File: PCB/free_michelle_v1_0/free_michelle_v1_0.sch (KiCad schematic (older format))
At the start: 2 parts

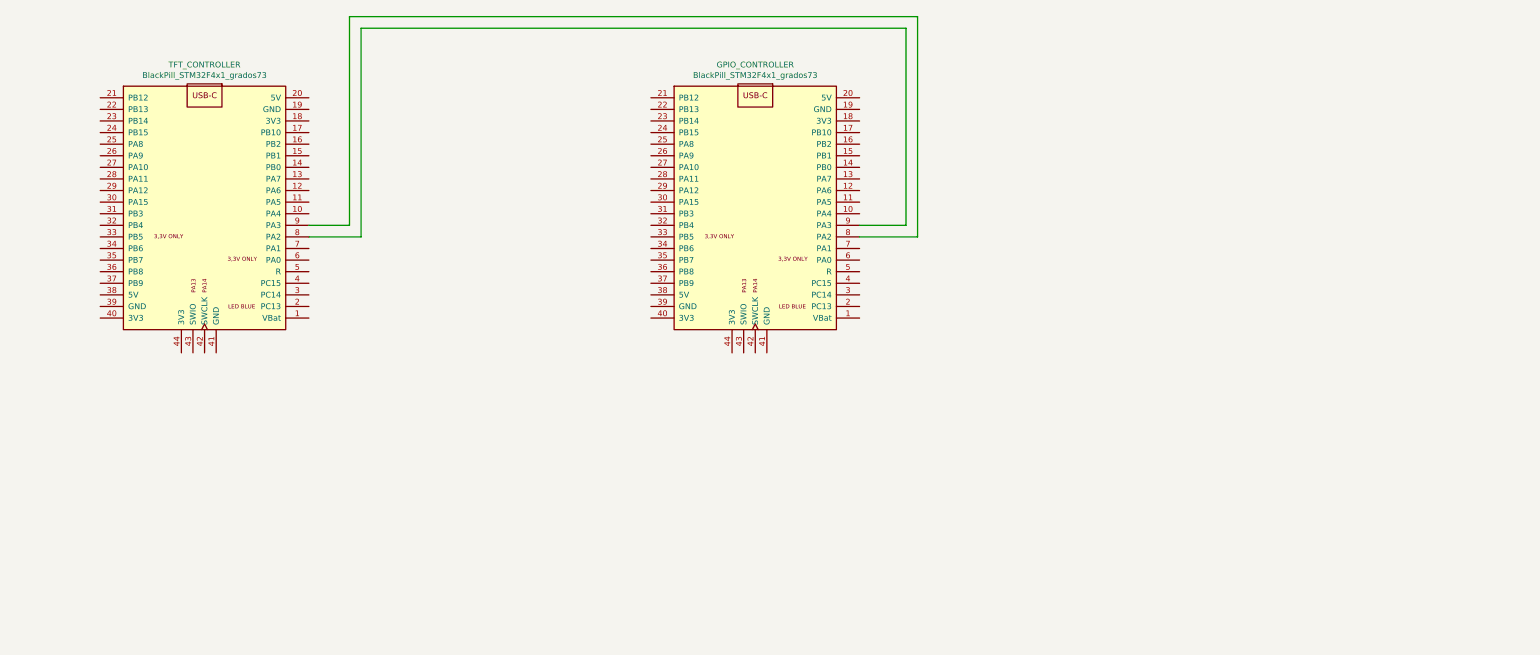
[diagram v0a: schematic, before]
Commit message: Dodano polaczenia pomiedzy uC a TFT
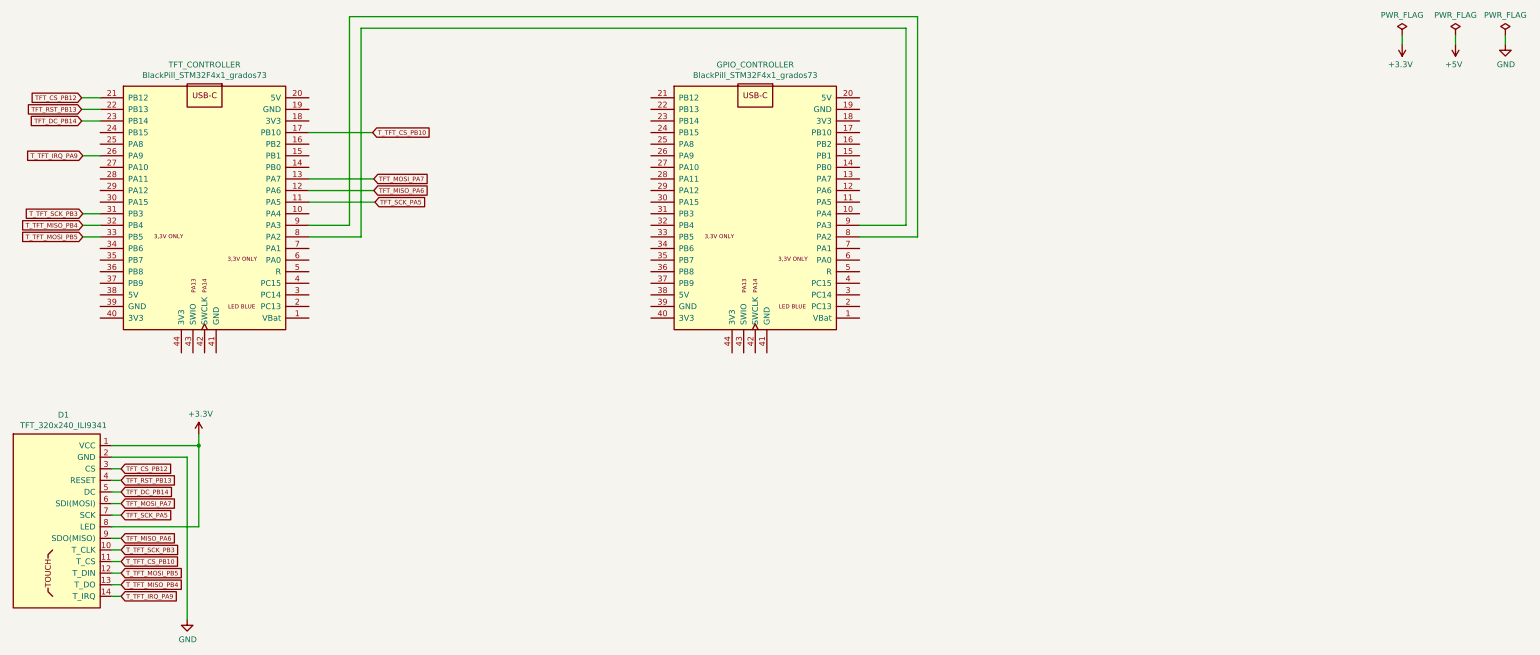
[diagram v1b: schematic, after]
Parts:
- added D1: TFT_320x240_ILI9341, symbol grad73_library:TFT_320x240_ILI9341
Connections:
- net TFT_SCK_PA5: now reaches TFT_CONTROLLER.11 (PA5)
- net TFT_SCK_PA5: now also D1.7 (SCK)
- net TFT_MISO_PA6: now reaches TFT_CONTROLLER.12 (PA6)
- net TFT_MISO_PA6: now also D1.9 (SDO(MISO))
- net TFT_MOSI_PA7: now reaches TFT_CONTROLLER.13 (PA7)
- net TFT_MOSI_PA7: now also D1.6 (SDI(MOSI))
- net T_TFT_CS_PB10: now reaches TFT_CONTROLLER.17 (PB10)
- net T_TFT_CS_PB10: now also D1.11 (T_CS)
- net TFT_CS_PB12: now reaches TFT_CONTROLLER.21 (PB12)
- net TFT_CS_PB12: now also D1.3 (CS)
- net TFT_RST_PB13: now reaches TFT_CONTROLLER.22 (PB13)
- net TFT_RST_PB13: now also D1.4 (RESET)
- net TFT_DC_PB14: now reaches TFT_CONTROLLER.23 (PB14)
- net TFT_DC_PB14: now also D1.5 (DC)
- net T_TFT_IRQ_PA9: now reaches TFT_CONTROLLER.26 (PA9)
- net T_TFT_IRQ_PA9: now also D1.14 (T_IRQ)
- net T_TFT_SCK_PB3: now reaches TFT_CONTROLLER.31 (PB3)
- net T_TFT_SCK_PB3: now also D1.10 (T_CLK)
- net T_TFT_MISO_PB4: now reaches TFT_CONTROLLER.32 (PB4)
- net T_TFT_MISO_PB4: now also D1.13 (T_DO)
- net T_TFT_MOSI_PB5: now reaches TFT_CONTROLLER.33 (PB5)
- net T_TFT_MOSI_PB5: now also D1.12 (T_DIN)
- new net +3V3: D1.1 (VCC), D1.8 (LED)
- new net GND: D1.2 (GND)
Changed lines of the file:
@@
 Wire Wire Line
 	8800 2800 8300 2800
+$Comp
+L grad73_library:TFT_320x240_ILI9341 D1
+U 1 1 61DB7F28
+P 1700 4400
+F 0 "D1" H 1433 4465 50  0000 C CNN
+F 1 "TFT_320x240_ILI9341" H 1433 4374 50  0000 C CNN
+F 2 "" H 1700 4400 50  0001 C CNN
+F 3 "" H 1700 4400 50  0001 C CNN
+	1    1700 4400
+	1    0    0    -1
+$EndComp
+$Comp
+L power:GND #PWR?
+U 1 1 61DBA788
+P 2500 6100
+F 0 "#PWR?" H 2500 5850 50  0001 C CNN
+F 1 "GND" H 2505 5927 50  0000 C CNN
+F 2 "" H 2500 6100 50  0001 C CNN
+F 3 "" H 2500 6100 50  0001 C CNN
+	1    2500 6100
+	1    0    0    -1
+$EndComp
+$Comp
+L power:+3.3V #PWR?
+U 1 1 61DBE35F
+P 2600 4500
+F 0 "#PWR?" H 2600 4350 50  0001 C CNN
+F 1 "+3.3V" H 2615 4673 50  0000 C CNN
+F 2 "" H 2600 4500 50  0001 C CNN
+F 3 "" H 2600 4500 50  0001 C CNN
+	1    2600 4500
+	1    0    0    -1
+$EndComp
+$Comp
+L power:PWR_FLAG #FLG?
+U 1 1 61DC06F2
+P 12980 1060
+F 0 "#FLG?" H 12980 1135 50  0001 C CNN
+F 1 "PWR_FLAG" H 12980 1233 50  0000 C CNN
+F 2 "" H 12980 1060 50  0001 C CNN
+F 3 "~" H 12980 1060 50  0001 C CNN
+	1    12980 1060
+	1    0    0    -1
+$EndComp
+$Comp
+L power:PWR_FLAG #FLG?
+U 1 1 61DC1287
+P 13440 1060
+F 0 "#FLG?" H 13440 1135 50  0001 C CNN
+F 1 "PWR_FLAG" H 13440 1233 50  0000 C CNN
+F 2 "" H 13440 1060 50  0001 C CNN
+F 3 "~" H 13440 1060 50  0001 C CNN
+	1    13440 1060
+	1    0    0    -1
+$EndComp
+$Comp
+L power:PWR_FLAG #FLG?
+U 1 1 61DC1D57
+P 13870 1060
+F 0 "#FLG?" H 13870 1135 50  0001 C CNN
+F 1 "PWR_FLAG" H 13870 1233 50  0000 C CNN
+F 2 "" H 13870 1060 50  0001 C CNN
+F 3 "~" H 13870 1060 50  0001 C CNN
+	1    13870 1060
+	1    0    0    -1
+$EndComp
+$Comp
+L power:+3.3V #PWR?
+U 1 1 61DC2834
+P 12980 1140
+F 0 "#PWR?" H 12980 990 50  0001 C CNN
+F 1 "+3.3V" H 12995 1313 50  0000 C CNN
+F 2 "" H 12980 1140 50  0001 C CNN
+F 3 "" H 12980 1140 50  0001 C CNN
+	1    12980 1140
+	-1   0    0    1
+$EndComp
+$Comp
+L power:+5V #PWR?
+U 1 1 61DC4ACB
+P 13440 1140
+F 0 "#PWR?" H 13440 990 50  0001 C CNN
+F 1 "+5V" H 13455 1313 50  0000 C CNN
+F 2 "" H 13440 1140 50  0001 C CNN
+F 3 "" H 13440 1140 50  0001 C CNN
+	1    13440 1140
+	-1   0    0    1
+$EndComp
+$Comp
+L power:GND #PWR?
+U 1 1 61DC5D3E
+P 13870 1140
+F 0 "#PWR?" H 13870 890 50  0001 C CNN
+F 1 "GND" H 13875 967 50  0000 C CNN
+F 2 "" H 13870 1140 50  0001 C CNN
+F 3 "" H 13870 1140 50  0001 C CNN
+	1    13870 1140
+	1    0    0    -1
+$EndComp
+Wire Wire Line
+	12980 1060 12980 1140
+Wire Wire Line
+	13440 1060 13440 1140
+Wire Wire Line
+	13870 1060 13870 1140
+Text GLabel 1930 4800 2    39   Input ~ 0
+TFT_CS_PB12
+Text GLabel 1590 1600 0    39   Input ~ 0
+TFT_CS_PB12
+Wire Wire Line
+	1590 1600 1750 1600
+Wire Wire Line
+	1850 4800 1930 4800
+Text GLabel 1930 4900 2    39   Input ~ 0
+TFT_RST_PB13
+Wire Wire Line
+	1850 4900 1930 4900
+Text GLabel 1590 1700 0    39   Input ~ 0
+TFT_RST_PB13
+Wire Wire Line
+	1590 1700 1750 1700
+Text GLabel 1930 5000 2    39   Input ~ 0
+TFT_DC_PB14
+Wire Wire Line
+	1930 5000 1850 5000
+Text GLabel 1590 1800 0    39   Input ~ 0
+TFT_DC_PB14
+Wire Wire Line
+	1590 1800 1750 1800
+Text GLabel 1930 5100 2    39   Input ~ 0
+TFT_MOSI_PA7
+Wire Wire Line
+	1930 5100 1850 5100
+Text GLabel 1930 5200 2    39   Input ~ 0
+TFT_SCK_PA5
+Wire Wire Line
+	1930 5200 1850 5200
+Text GLabel 4110 2300 2    39   Input ~ 0
+TFT_MOSI_PA7
+Wire Wire Line
+	4110 2300 3550 2300
+Text GLabel 4120 2500 2    39   Input ~ 0
+TFT_SCK_PA5
+Wire Wire Line
+	4120 2500 3550 2500
+Wire Wire Line
+	1850 4600 2600 4600
+Wire Wire Line
+	2600 4600 2600 4500
+Wire Wire Line
+	1850 5300 2600 5300
+Wire Wire Line
+	2600 5300 2600 4600
+Connection ~ 2600 4600
+Text GLabel 1930 5400 2    39   Input ~ 0
+TFT_MISO_PA6
+Wire Wire Line
+	1930 5400 1850 5400
+Text GLabel 4110 2400 2    39   Input ~ 0
+TFT_MISO_PA6
+Wire Wire Line
+	4110 2400 3550 2400
+Text GLabel 1930 5500 2    39   Input ~ 0
+T_TFT_SCK_PB3
+Wire Wire Line
+	1930 5500 1850 5500
+Text GLabel 1930 5600 2    39   Input ~ 0
+T_TFT_CS_PB10
+Text GLabel 1930 5700 2    39   Input ~ 0
+T_TFT_MOSI_PB5
+Text GLabel 1930 5800 2    39   Input ~ 0
+T_TFT_MISO_PB4
+Text GLabel 1930 5900 2    39   Input ~ 0
+T_TFT_IRQ_PA9
+Wire Wire Line
+	1930 5600 1850 5600
+Wire Wire Line
+	1930 5700 1850 5700
+Wire Wire Line
+	1930 5800 1850 5800
+Wire Wire Line
+	1930 5900 1850 5900
+Text GLabel 1600 2600 0    39   Input ~ 0
+T_TFT_SCK_PB3
+Text GLabel 4100 1900 2    39   Input ~ 0
+T_TFT_CS_PB10
+Text GLabel 1600 2800 0    39   Input ~ 0
+T_TFT_MOSI_PB5
+Text GLabel 1600 2700 0    39   Input ~ 0
+T_TFT_MISO_PB4
+Text GLabel 1600 2100 0    39   Input ~ 0
+T_TFT_IRQ_PA9
+Wire Wire Line
+	1600 2100 1750 2100
+Wire Wire Line
+	1600 2600 1750 2600
+Wire Wire Line
+	1600 2700 1750 2700
+Wire Wire Line
+	1600 2800 1750 2800
+Wire Wire Line
+	4100 1900 3550 1900
+Wire Wire Line
+	2500 6100 2500 4700
+Wire Wire Line
+	2500 4700 1850 4700
 $EndSCHEMATC
